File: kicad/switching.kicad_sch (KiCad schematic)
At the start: 7 parts

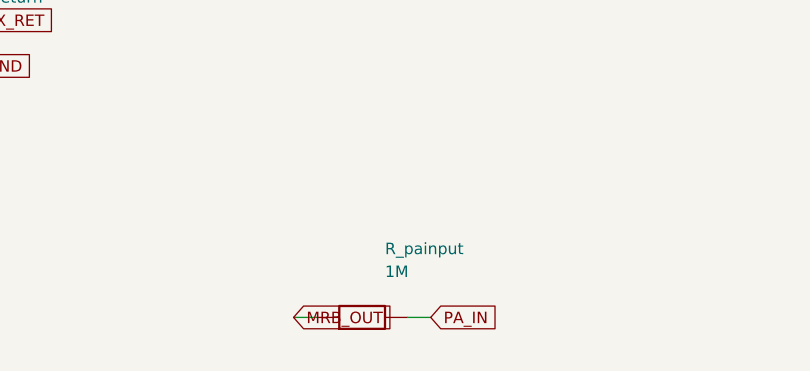
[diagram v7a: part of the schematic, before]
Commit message: Redesign effects chain: active reverb summer + output buffer + split bias
Resolves roast R3 (broken passive mixer) and R6 (shared VBIAS bleed), using the
two spare TL072 halves and verifying with a rail-aware SPICE model.

- Reverb wet/dry mix is now an ACTIVE inverting summer on IC1-B (dry always on,
  wet via POT_REV, unity each, low-Z out about VBIAS_R). Removed the broken
  passive R_dry_tap/R_blend1/R_blend2 (1M dry series made it ~all-wet into an
  unbuffered 110k node).
- IC2-B repurposed as the post-MRB OUTPUT BUFFER driving PA_IN (removed the
  unbuffered R_painput 1M and a dead C_trem_out/R_trem_pass branch).
- VBIAS split into independent VBIAS_R (reverb) and VBIAS_T (tremolo) dividers
  (100k/100k + 47uF each) -> the LFO can no longer modulate the reverb reference.

Verification: new models/opamp_rail.sub clamps the output to the rails (unlike
opamp1p.sub), and spice/tran_reverb_mixer.cir confirms on a single +17V supply:
mid-rail bias 8.50 V, unity (0.0 dB) sum, clips at 15.5/1.5 V -> +-7 V headroom
(~24 dB over a 0.42 V program peak). This is the large-signal/headroom check the
rail-less model could not do (roast R7).

ERC 0; demo DRC 0; full board regenerated (106 footprints); run_all.sh exit 0;
BOM + roast doc + SCHEMATIC-BUILD + spice/README + CHANGELOG updated.

https://claude.ai/code/session_01PkrfUi9tvZfLvudJ7h23qD
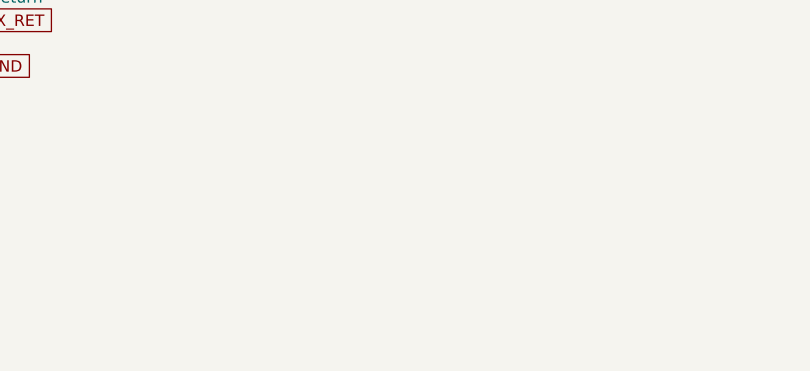
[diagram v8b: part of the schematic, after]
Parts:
- removed R_painput: 1M, Resistor_THT:R_Axial_DIN0207_L6.3mm_D2.5mm_P5.08mm_Vertical, symbol cr_primitives:R
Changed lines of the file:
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@@
     (pin "1")
     (pin "2")
-    (instances (project "cambridge_reverb" (path "/0afdd53e-4713-41fb-bc93-93ba1769810d" (reference "J_IN1") (unit 1))))
+    (instances (project "cambridge_reverb" (path "/ec396f92-9d29-4422-98c6-cdef3d2a4505" (reference "J_IN1") (unit 1))))
   )
   (wire (pts (xy 139.7 93.97999999999999) (xy 142.24 93.97999999999999)) (stroke (width 0) (type default)))
@@
     (pin "1")
     (pin "2")
-    (instances (project "cambridge_reverb" (path "/0afdd53e-4713-41fb-bc93-93ba1769810d" (reference "J_IN2") (unit 1))))
+    (instances (project "cambridge_reverb" (path "/ec396f92-9d29-4422-98c6-cdef3d2a4505" (reference "J_IN2") (unit 1))))
   )
   (wire (pts (xy 139.7 124.46) (xy 142.24 124.46)) (stroke (width 0) (type default)))
@@
     (pin "1")
     (pin "2")
-    (instances (project "cambridge_reverb" (path "/0afdd53e-4713-41fb-bc93-93ba1769810d" (reference "J_IN3") (unit 1))))
+    (instances (project "cambridge_reverb" (path "/ec396f92-9d29-4422-98c6-cdef3d2a4505" (reference "J_IN3") (unit 1))))
   )
   (wire (pts (xy 139.7 153.67) (xy 142.24 153.67)) (stroke (width 0) (type default)))
@@
     (pin "5")
     (pin "6")
-    (instances (project "cambridge_reverb" (path "/0afdd53e-4713-41fb-bc93-93ba1769810d" (reference "FS1") (unit 1))))
+    (instances (project "cambridge_reverb" (path "/ec396f92-9d29-4422-98c6-cdef3d2a4505" (reference "FS1") (unit 1))))
   )
   (wire (pts (xy 217.17000000000002 119.38) (xy 214.63000000000002 119.38)) (stroke (width 0) (type default)))
@@
     (pin "1")
     (pin "2")
-    (instances (project "cambridge_reverb" (path "/0afdd53e-4713-41fb-bc93-93ba1769810d" (reference "LS1") (unit 1))))
+    (instances (project "cambridge_reverb" (path "/ec396f92-9d29-4422-98c6-cdef3d2a4505" (reference "LS1") (unit 1))))
   )
   (wire (pts (xy 279.4 184.15000000000003) (xy 276.86 184.15000000000003)) (stroke (width 0) (type default)))
@@
     (pin "1")
     (pin "2")
-    (instances (project "cambridge_reverb" (path "/0afdd53e-4713-41fb-bc93-93ba1769810d" (reference "R_spk_rtn") (unit 1))))
+    (instances (project "cambridge_reverb" (path "/ec396f92-9d29-4422-98c6-cdef3d2a4505" (reference "R_spk_rtn") (unit 1))))
   )
   (wire (pts (xy 240.03 186.69) (xy 237.49 186.69)) (stroke (width 0) (type default)))
@@
   (wire (pts (xy 250.19000000000003 186.69) (xy 252.73000000000002 186.69)) (stroke (width 0) (type default)))
   (global_label "GND" (shape input) (at 252.73000000000002 186.69 0) (fields_autoplaced) (effects (font (size 1.27 1.27)) (justify left)))
-  (symbol (lib_id "cr_primitives:R") (at 185.42000000000002 186.69 0) (unit 1)
-    (in_bom yes) (on_board yes) (dnp no)
-    (property "Reference" "R_painput" (at 187.96 179.07 0) (effects (font (size 1.27 1.27)) (justify left)))
-    (property "Value" "1M" (at 187.96 181.60999999999999 0) (effects (font (size 1.27 1.27)) (justify left)))
-    (property "Footprint" "Resistor_THT:R_Axial_DIN0207_L6.3mm_D2.5mm_P5.08mm_Vertical" (at 185.42000000000002 186.69 0) (effects (font (size 1.27 1.27)) hide))
-    (pin "1")
-    (pin "2")
-    (instances (project "cambridge_reverb" (path "/0afdd53e-4713-41fb-bc93-93ba1769810d" (reference "R_painput") (unit 1))))
-  )
-  (wire (pts (xy 180.34 186.69) (xy 177.8 186.69)) (stroke (width 0) (type default)))
-  (global_label "MRB_OUT" (shape input) (at 177.8 186.69 180) (fields_autoplaced) (effects (font (size 1.27 1.27)) (justify left)))
-  (wire (pts (xy 190.5 186.69) (xy 193.04000000000002 186.69)) (stroke (width 0) (type default)))
-  (global_label "PA_IN" (shape input) (at 193.04000000000002 186.69 0) (fields_autoplaced) (effects (font (size 1.27 1.27)) (justify left)))
   (sheet_instances (path "/" (page "1")))
 )
